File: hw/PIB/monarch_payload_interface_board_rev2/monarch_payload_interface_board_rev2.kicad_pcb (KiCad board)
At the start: 4 copper layers, 96 x 89.9 mm, 187 parts, among them J1 5037630291, J10 5037630491, J11 5037630691, J12 5037630691, J13 5037630491, J14 5037630491, J15 5037630691, J16 20021121-00008C4LF, J2 5037630291, J3 5037630691, J4 5037630691, J5 5037630691, J6 5037630691, J7 5037630691, J8 5037630691, J9 5037630491, Q1 FZT600TA, Q10 FZT600TA, Q11 FZT600TA, Q12 FZT600TA, Q13 FZT600TA, Q14 FZT600TA, Q15 FZT600TA, Q16 FZT600TA, Q17 FZT600TA, Q18 FZT600TA, Q19 FZT600TA, Q2 FZT600TA, Q3 FZT600TA, Q4 FZT600TA, Q5 FZT600TA, Q6 FZT600TA, Q7 FZT600TA, Q8 FZT600TA, Q9 FZT600TA, U1 Payload, U10 AD7124-8BCPZ-RL, U11 WSK06121L000FEA, U12 WSK06121L000FEA, U13 WSK06121L000FEA, U14 WSK06121L000FEA, U2 STM32L4A6VGTx, U3 MAX31856MUD_T, U4 TPS61088QRHLRQ1, U5 MAX31856MUD_T, U6 MAX31856MUD_T, U7 MAX31856MUD_T, U8 MAX31856MUD_T, U9 AD7124-8BCPZ-RL

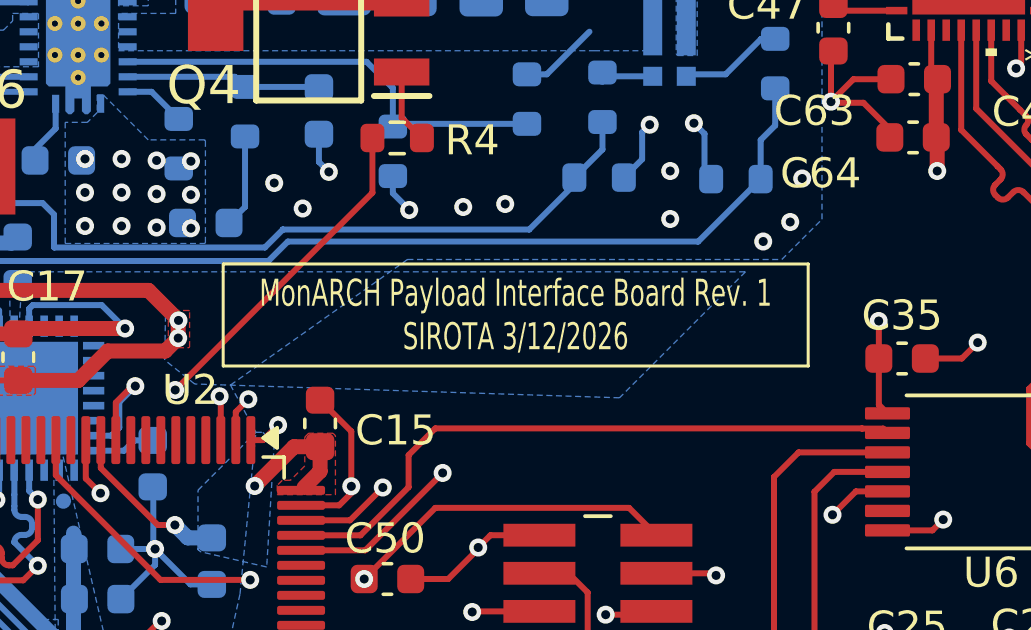
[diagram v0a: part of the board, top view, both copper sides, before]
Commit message: MCU Power Pins Fix
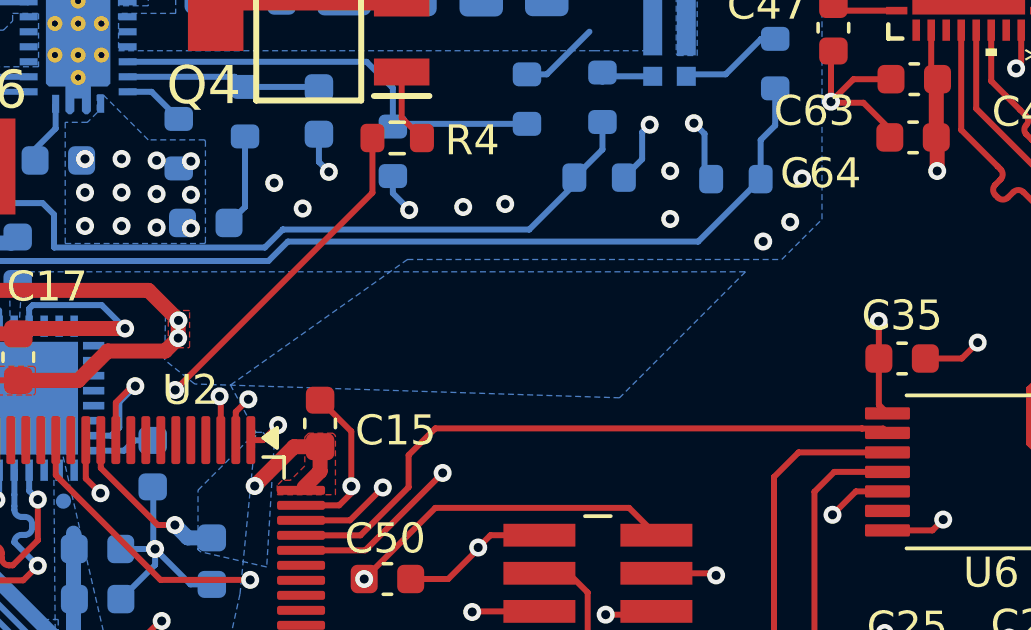
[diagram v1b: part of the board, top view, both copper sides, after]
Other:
- board text removed: "MonARCH Payload Interface Board Rev. 1 SIROTA 3/12/2026"

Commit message: Connector Additions
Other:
- board text added: "MonARCH Payload Interface Board Rev. 2"
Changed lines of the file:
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@@
+		)
+	)
+	(gr_rect
+		(start 68.25 47)
+		(end 87.75 50.4)
+		(stroke
+			(width 0.1)
+			(type default)
+		)
+		(fill no)
+		(layer "F.SilkS")
+	)
+	(gr_text "MonARCH Payload Interface Board Rev. 2\n"
+		(at 78 48.7 0)
+		(layer "F.SilkS")
+		(effects
+			(font
+				(size 0.9 0.6)
+				(thickness 0.15)
+			)
+			(justify bottom)
 		)
 	)
